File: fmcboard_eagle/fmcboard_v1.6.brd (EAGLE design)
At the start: 147 x 74 mm, 239 parts, among them IC1 OPA695IDR, IC10 LM358, IC11 7805DT, IC12 SN74AUC2G66DCTR, IC13 SN74AUC2G66DCTR, IC14 SN74AUC2G66DCTR, IC15 SN74AUC2G66DCTR, IC16 DAC7578SPWR, IC17 SN74AUC2G66DCTR, IC18 SN74AUC2G66DCTR, IC19 SN74AUC2G66DCTR, IC2 DAC7578SPWR, IC20 SN74AUC2G66DCTR, IC21 74AUP2GU04GW, IC22 74AUP2GU04GW, IC23 74AUP2GU04GW, IC24 74AUP2GU04GW, IC25 MC7905ACD2TR4G, IC26 AMS1117-1.8, IC27 OPA699ID, IC29 LM337KVURG3, IC3 LTC6229IMS8E#TRPBF, IC4 OPA695IDR, IC5 LTC6229IMS8E#TRPBF, IC6 OPA695IDR, IC7 OPA699ID, IC8 LM358, IC9 LM358, J1 8pin, J11 4p-2.54, J12 4p-2.54, J13 4p-2.54, J14 4p-2.54, J2 ASP-134604-01, J3 4p-2.54, J4 4p-2.54, J5 4p-2.54, J6 4p-2.54, J7 4p-2.54, J8 4p-2.54, J9 8pin, U1 TXS0108EPWR

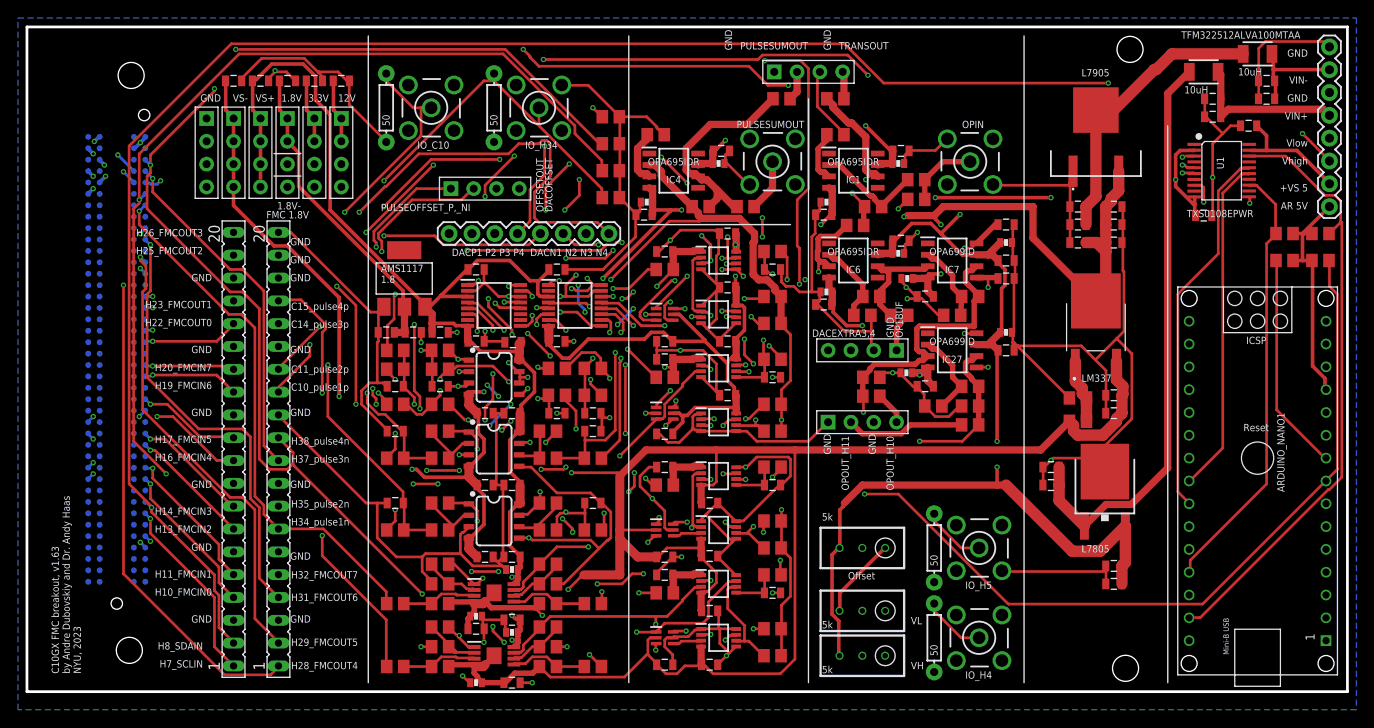
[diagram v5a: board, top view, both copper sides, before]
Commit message: -1.8V 100uF cap for stability 330 -> 470 for 695 pulseout 330 -> 470 for inputs to pulseout Replace initial 695 with 699 for lower noise, and feedback 470 to 1k Increase gain for opbuf and h10, 470 -> 1k Remove h11 100 -> 10 ohm before h10 h11 pulseout probe points
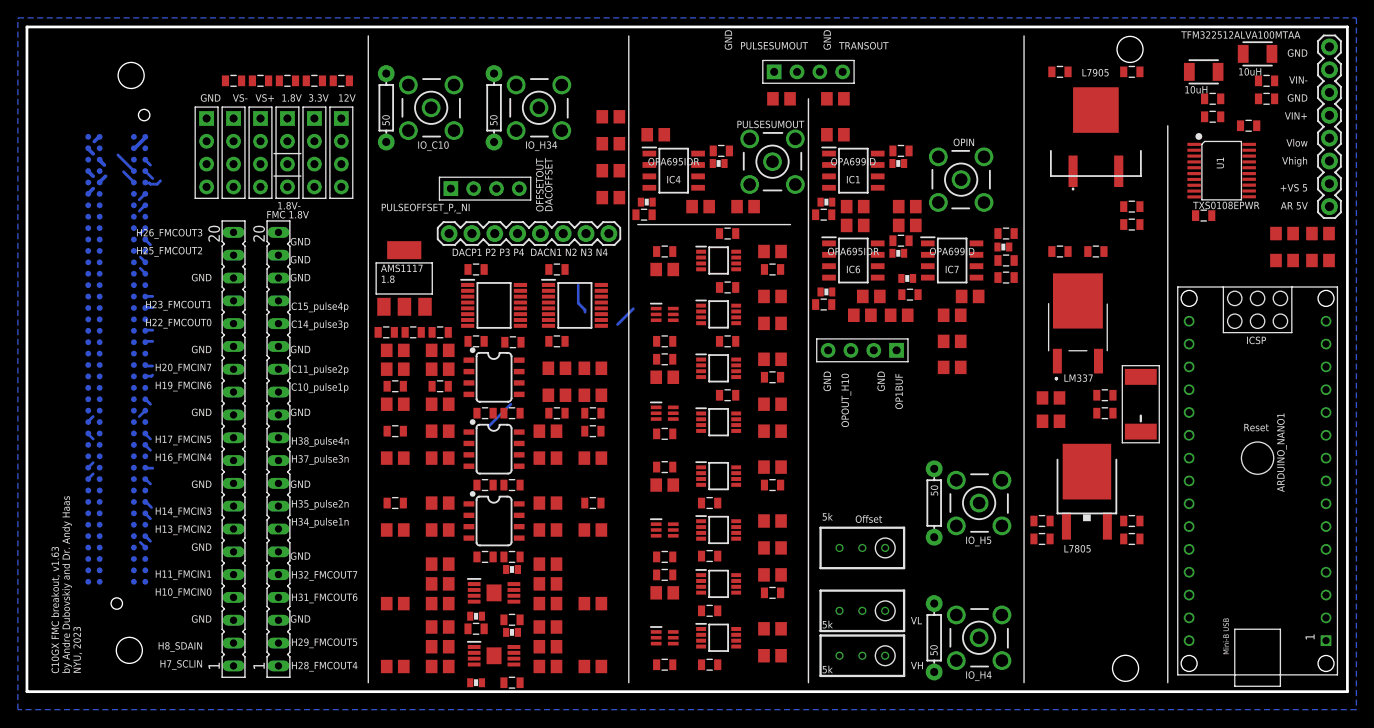
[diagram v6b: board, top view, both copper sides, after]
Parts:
- removed C30, C31: 0.1uF, SparkFun-Passives:0805
- removed C89, C90: 100pF, passives:0603_CAP
- removed IC27: OPA699ID, OPA699ID:SOIC127P600X175-8N
- removed J14: 4p-2.54, Seeed-Connector:H4-2.54
- removed R10, R78, R87: 100, rcl:R0805
- removed R9: 470, rcl:R0805
- added C95: 100uF, SparkFun-Passives:VISHAY_C
- IC1: value OPA695IDR -> OPA699ID; device OPA695IDR:SOIC127P600X175-8N -> OPA699ID:SOIC127P600X175-8N
- R1, R12, R32, R33, R36, R38, R40, R7, R8: value 330 -> 470
- R11, R18, R6: value 470 -> 1k
- R20: value 100 -> 47
- R25, R31: value 470 -> 330
- R3, R71, R72, R86, R89: value 100 -> 10
- R88: value 1k -> 10
- moved C40 18.0 mm to (123.0, 69.0), turned to 180 degrees
- moved C45 15.1 mm to (115.0, 69.0)
- moved R88 9.85 mm to (103.0, 39.0), turned to 0 degrees
- moved R86 9.55 mm to (103.0, 36.1), turned to 0 degrees
- moved C87 9.50 mm to (108.7, 49.5)
- moved C2 6.08 mm to (113.0, 17.0)
- moved C43 6.08 mm to (113.0, 19.0)
- moved C38 5.39 mm to (123.0, 17.0), turned to 0 degrees
- moved C47 5.39 mm to (123.0, 19.0), turned to 0 degrees
- moved IO_H5 5.00 mm to (106.0, 21.0)
- moved R16 5.00 mm to (101.0, 21.0), turned to 270 degrees
- moved R2 3.16 mm to (98.0, 54.0)
- moved R42 3.07 mm to (98.0, 51.9)
- moved R14 3.00 mm to (114.0, 30.1)
- moved R70 3.00 mm to (114.0, 32.7)
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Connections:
- removed net DACEXTRA3: IC16.12, J5.3
- removed net DACEXTRA4: IC16.6, J5.4
- removed net N$1: IC27.2, R10.2, R9.1
- removed net N$41: J14.4, R86.1
- new net OP2OUT: IC7.6, R6.2, R88.2
- net 1V8-: now also C95.-
- net GND: now also C95.+, J5.4; no longer C30.2, C31.2, C89.2, C90.2, J14.1, J14.3, R10.1, R87.1, R88.1
- net N$40: now also J5.3, R86.1; no longer J14.2, R78.1
- net OPOUT_H10: now also R88.1; no longer IC27.3, IC7.6, R6.2, R88.2
- net OPOUT_H11: no longer IC27.6, R78.2, R87.2, R9.2
- net VH: no longer IC27.8
- net VL: no longer IC27.5
- net VS+: no longer C30.1, C89.1, IC27.7
- net VS-: no longer C31.1, C90.1, IC27.4
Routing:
- net GND: track 634.2 -> 2.24 mm, vias 37 -> 0
- net VS+: track 390.6 -> 0.00 mm, vias 8 -> 0
- net 1V8-: track 278.4 -> 0.00 mm, vias 3 -> 0
- net VS-: track 268.2 -> 0.00 mm, vias 11 -> 0
- net 1V8: track 218.4 -> 0.00 mm, vias 5 -> 0
- net SDAIN: track 189.7 -> 0.96 mm, vias 3 -> 0
- net AR_SCLIN2: track 183.8 -> 0.00 mm, vias 5 -> 0
- net SCLIN: track 163.7 -> 0.84 mm, vias 2 -> 0
- net H35: track 161.1 -> 0.95 mm, vias 5 -> 0
- net H38: track 153.7 -> 0.83 mm, vias 7 -> 0
- net AR_SDAIN2: track 151.5 -> 0.00 mm, vias 8 -> 0
- net OPOUT_H10: track 142.8 -> 0.79 mm, vias 2 -> 0
- net H37: track 138.7 -> 1.17 mm, vias 3 -> 0
- net C10: track 132.2 -> 0.81 mm, vias 10 -> 0
- net G36: track 132.7 -> 1.66 mm, vias 4 -> 0
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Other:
- board text removed: "DACEXTRA3,4"
- board text removed: "OPOUT_H11"

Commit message: v1.64 add test 2.6k resistor routed, better gnd connections
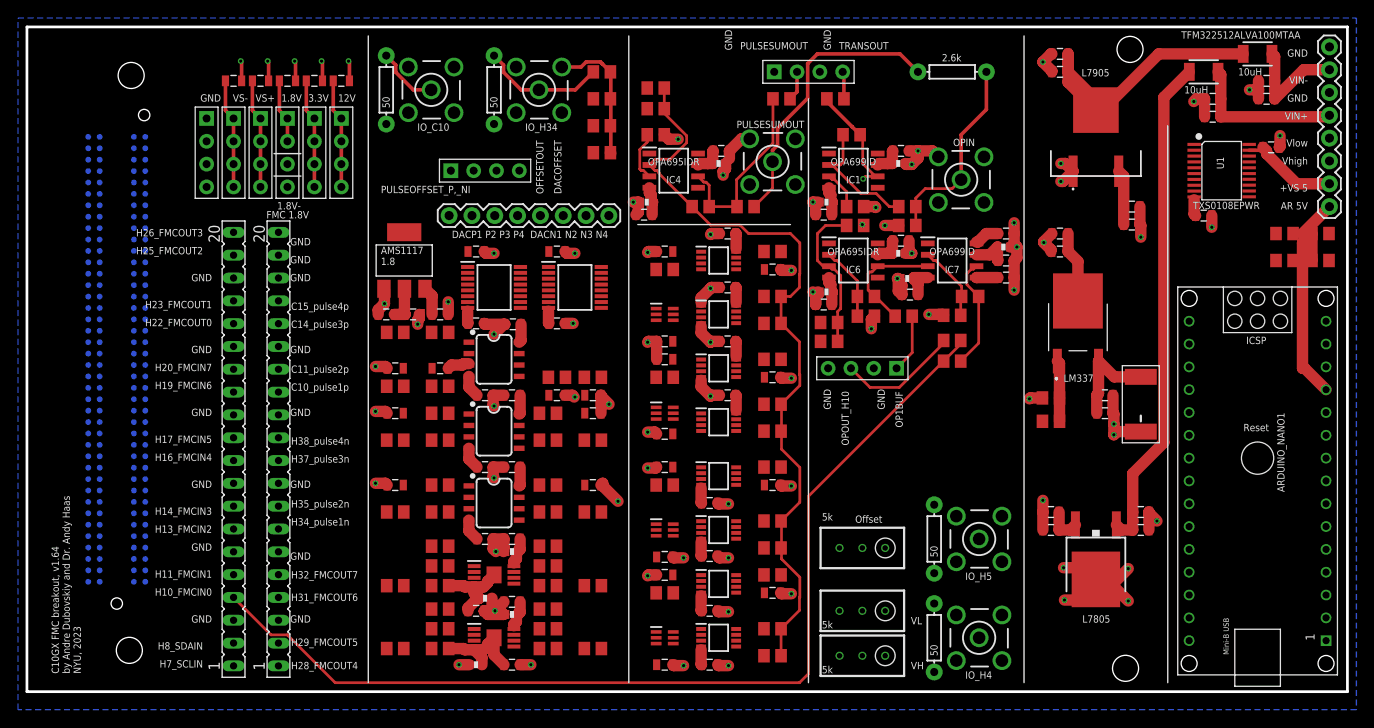
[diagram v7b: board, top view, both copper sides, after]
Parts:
- added R9: 2.6k, SparkFun-Resistors:AXIAL-0.3
- R13: value 100 -> 10
- moved R79 42.7 mm to (70.0, 67.2), turned to 180 degrees
- moved R85 37.6 mm to (70.0, 64.9)
- moved R25 30.7 mm to (89.3, 41.1)
- moved R31 26.5 mm to (89.3, 39.0)
- moved R80 14.0 mm to (64.0, 69.0)
- moved C2 11.4 mm to (124.0, 20.0), turned to 0 degrees
- moved C43 11.0 mm to (124.0, 18.0), turned to 0 degrees
- moved C38 9.49 mm to (114.0, 20.0), turned to 180 degrees
- moved C47 9.06 mm to (114.0, 18.0), turned to 180 degrees
- moved R3 8.30 mm to (92.2, 54.0)
- moved C40 8.25 mm to (115.0, 71.0), turned to 0 degrees
- moved R81 8.06 mm to (64.0, 66.0)
- moved R11 8.01 mm to (91.8, 62.0), turned to 180 degrees
- moved IC11 7.07 mm to (119.0, 15.0), turned to 180 degrees
- moved C33 4.00 mm to (115.0, 49.0), turned to 180 degrees
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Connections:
- removed net N$18: PULSESUMOUT.1, R34.2
- new net PULSEOUT: PULSESUMOUT.1, R34.2, R9.P$2
- net IO1: now also R9.P$1
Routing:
- net GND: track 2.24 -> 196.8 mm, vias 0 -> 77
- net OPOUT_H10: track 0.79 -> 112.5 mm
- net PULSESUMIN: track 0.00 -> 85.3 mm
- net VS+: track 0.00 -> 57.6 mm
- net VIN+CLEAN: track 0.00 -> 55.7 mm
- net AR_5V: track 0.00 -> 50.4 mm
- net VS-: track 0.00 -> 47.4 mm
- net 1V8-: track 0.00 -> 38.4 mm
- net VIN-CLEAN: track 0.00 -> 35.1 mm
- net PULSEOUT: track 0.00 -> 31.9 mm
- net IO1: track 0.00 -> 22.1 mm
- net 1V8: track 0.00 -> 21.1 mm
- net PULSESUMOUT: track 0.00 -> 20.8 mm
- net TRANSOUT: track 0.00 -> 18.5 mm, vias 0 -> 2
- net N$10: track 0.00 -> 17.4 mm
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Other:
- board text added: "C10GX FMC breakout, v1.64 by Andre Dubovskiy and Dr. Andy Haas NYU, 2023"
- board text removed: "C10GX FMC breakout, v1.63 by Andre Dubovskiy and Dr. Andy Haas NYU, 2023"

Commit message: v1.64
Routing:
- net VS+: track 57.6 -> 339.0 mm, vias 0 -> 9
- net VS-: track 47.4 -> 241.9 mm, vias 0 -> 7
- net AR_SDAIN2: track 0.00 -> 191.8 mm, vias 0 -> 7
- net 1V8-: track 38.4 -> 223.5 mm, vias 0 -> 3
- net SDAIN: track 0.00 -> 172.6 mm, vias 0 -> 4
- net AR_SCLIN2: track 0.00 -> 171.4 mm, vias 0 -> 5
- net SCLIN: track 0.00 -> 162.7 mm, vias 0 -> 3
- net H38: track 0.00 -> 159.3 mm, vias 0 -> 4
- net 1V8: track 21.1 -> 175.5 mm, vias 0 -> 6
- net C10: track 7.05 -> 157.7 mm, vias 0 -> 1
- net DACP3: track 0.00 -> 141.2 mm, vias 0 -> 5
- net H35: track 0.00 -> 137.7 mm, vias 0 -> 6
- net G37: track 0.00 -> 136.8 mm, vias 0 -> 3
- net G36: track 0.00 -> 135.8 mm, vias 0 -> 4
- net H37: track 0.00 -> 127.8 mm, vias 0 -> 3
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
